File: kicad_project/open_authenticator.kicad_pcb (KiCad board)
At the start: 2 copper layers, 82 x 42 mm, 64 parts, among them IC1 TPS22919DCKR, J1 Conn_01x02_Female, J2 TYPE-C-31-M-17, J3 Conn_01x02_Female, P1 SSD1306_ribbon, Q1 DMP2305U-7, SW1 UP, SW2 DOWN, SW3 BOOT/SELECT, SW4 RESET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

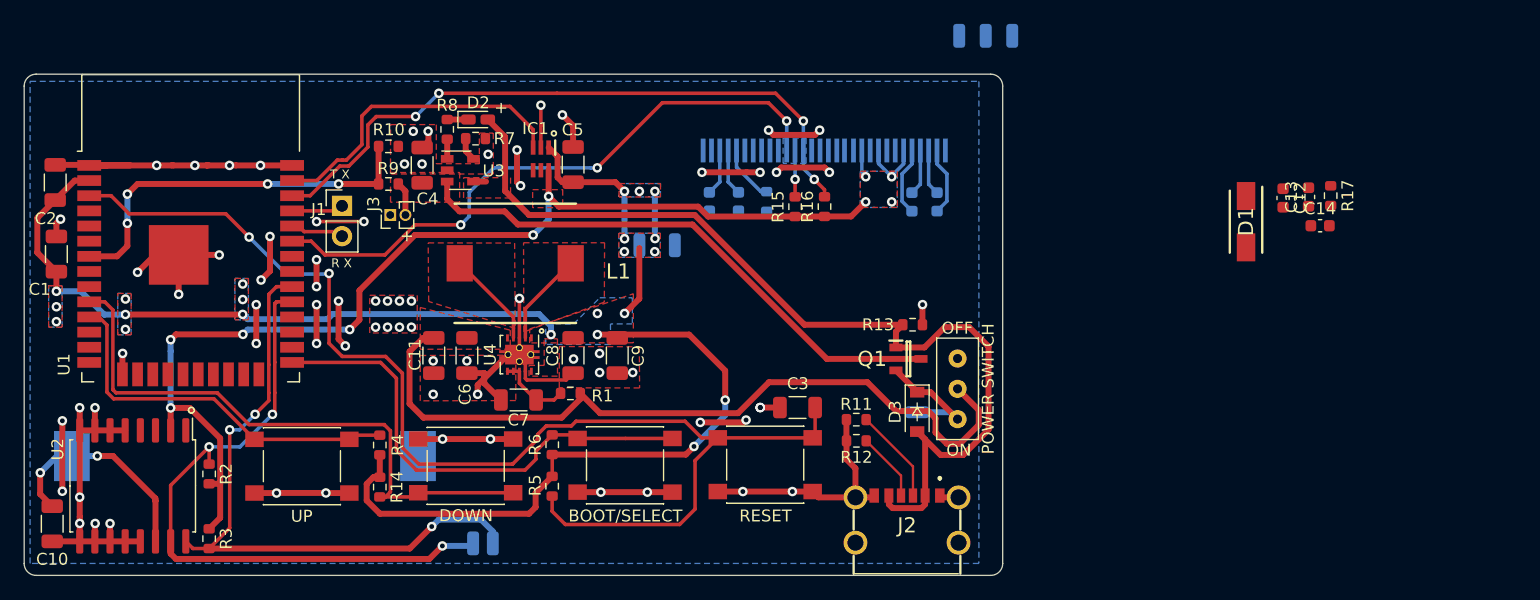
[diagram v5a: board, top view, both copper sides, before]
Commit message: Routed components of OLED sub circuit, optimised routing further (major: removed 3v3 line going under the regulator
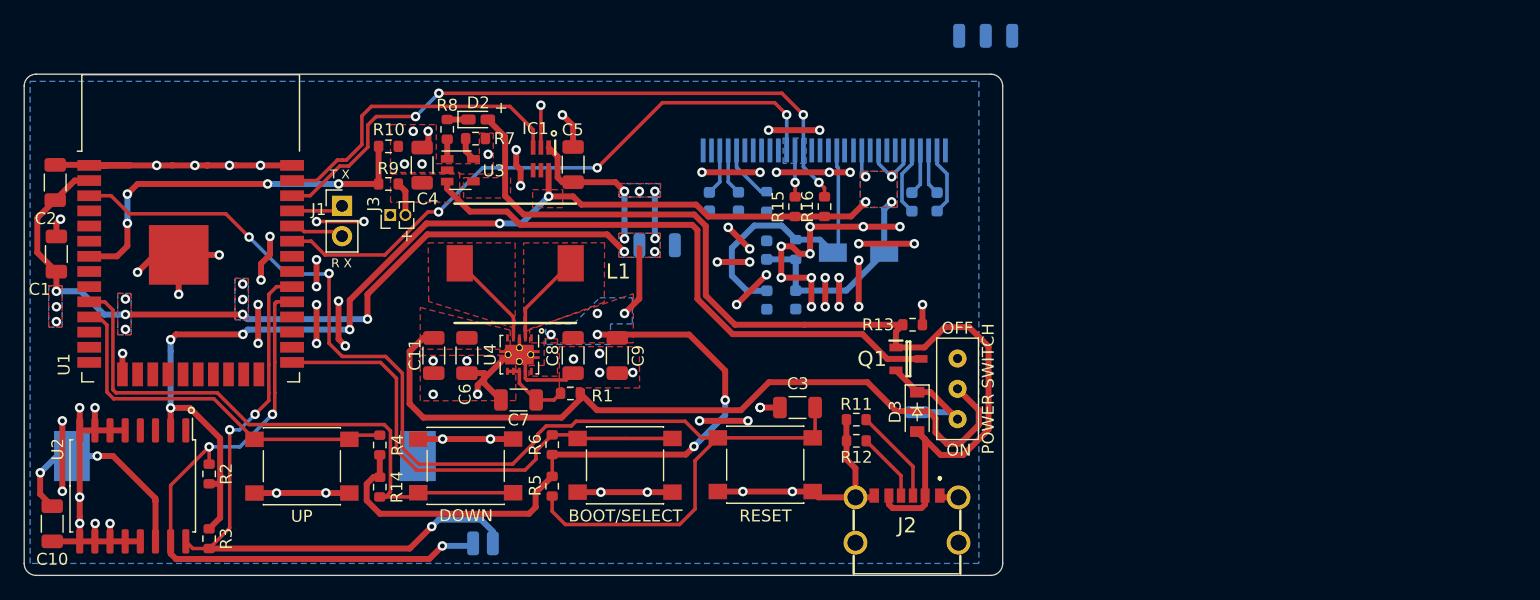
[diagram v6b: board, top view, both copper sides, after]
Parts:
- C12, C13, C14, D1, R17: moved to B.Cu
- moved C14 46.8 mm to (152.2, 98.9), turned to 90 degrees
- moved R17 45.1 mm to (154.7, 94.7), turned to 90 degrees
- moved C13 43.8 mm to (154.7, 98.9)
- moved C12 43.5 mm to (152.2, 94.7), turned to 90 degrees
- moved D1 32.6 mm to (159.9, 95.0), turned to 180 degrees
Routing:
- net GND: track 192.3 -> 232.6 mm, vias 74 -> 88
- net Net-(C14-Pad2): track 0.00 -> 24.8 mm
- net /LOAD_SWITCH_VCC: track 98.6 -> 115.7 mm
- net +3V3: track 135.3 -> 144.9 mm, vias 22 -> 23
- net +BATT: track 49.9 -> 52.8 mm
- net VBUS: track 82.0 -> 84.6 mm
- net /IO21_SDA: track 55.4 -> 54.5 mm

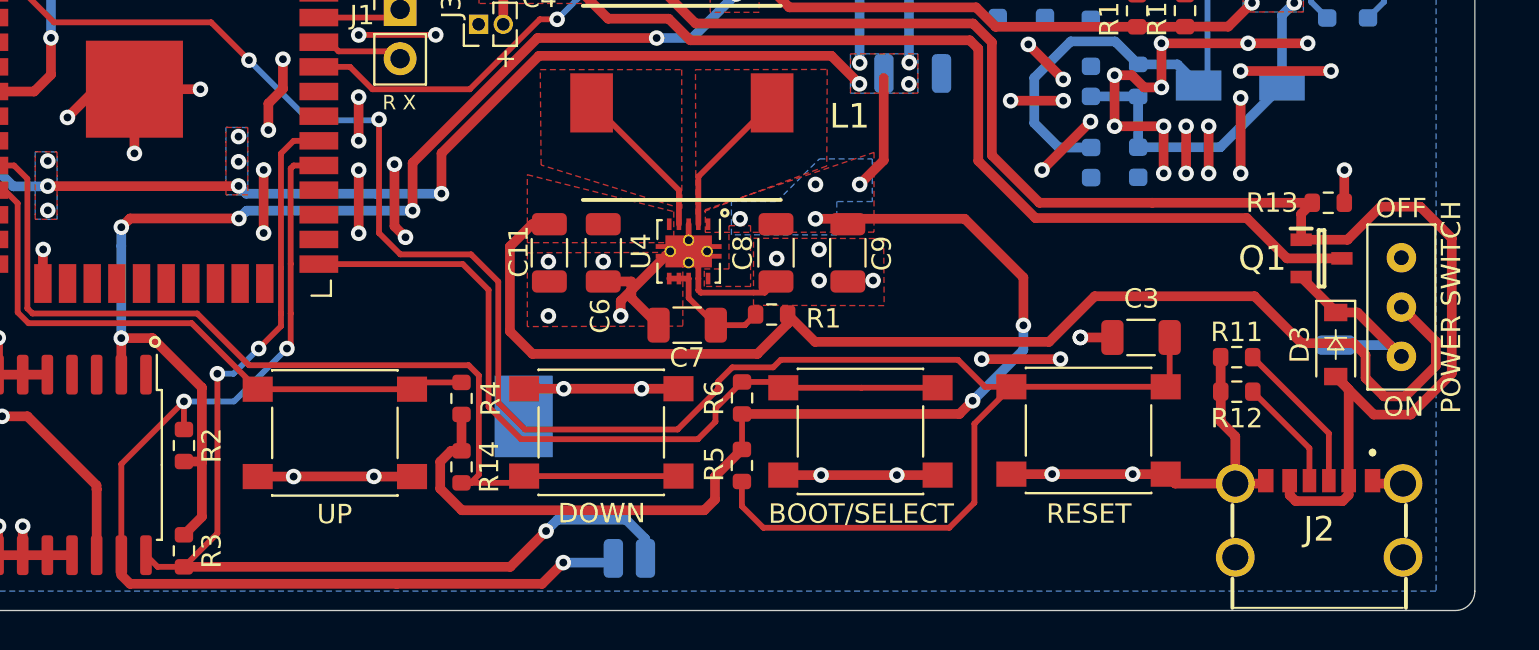
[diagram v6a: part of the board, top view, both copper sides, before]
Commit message: Optimised routing near slide switch
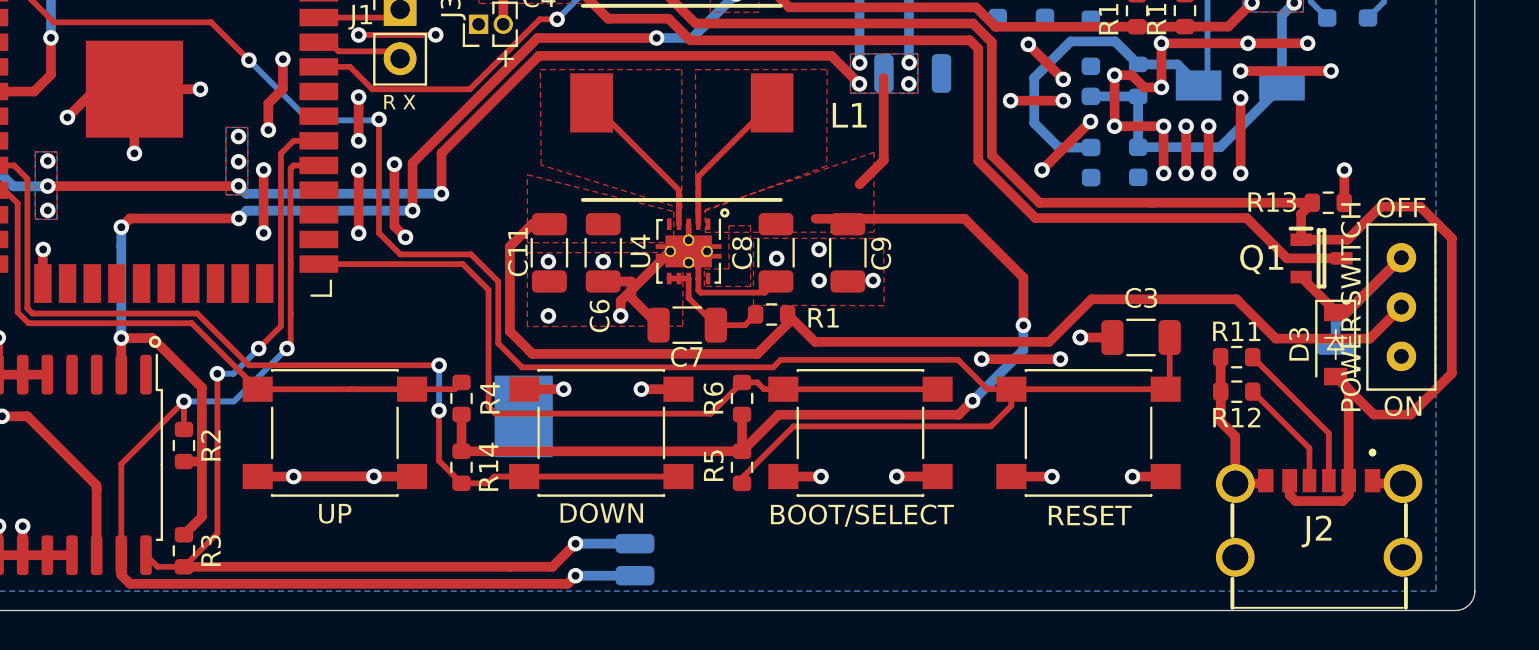
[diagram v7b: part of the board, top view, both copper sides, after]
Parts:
- moved TP2 1.42 mm to (128.7, 120.2), turned to 90 degrees
- moved TP3 0.93 mm to (128.7, 118.6), turned to 90 degrees
- moved SW4 0.12 mm to (152.1, 112.8)
- moved R5 0.09 mm to (134.2, 114.6)
- moved SW3 0.07 mm to (140.3, 112.8)
- turned SW5 to 0 degrees
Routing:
- net GND: track 232.6 -> 216.7 mm
- net /EN: track 103.6 -> 94.0 mm
- net Net-(C11-Pad1): track 65.0 -> 57.4 mm
- net +3V3: track 144.9 -> 139.4 mm, vias 23 -> 19
- net /V_INPUT: track 10.5 -> 13.0 mm
- net /IO18_SCL: track 54.5 -> 52.0 mm
- net /IO25: track 51.1 -> 49.3 mm, vias 0 -> 2
- net /BOOT: track 40.9 -> 39.8 mm
- net /IO5_SDA: track 55.1 -> 55.9 mm

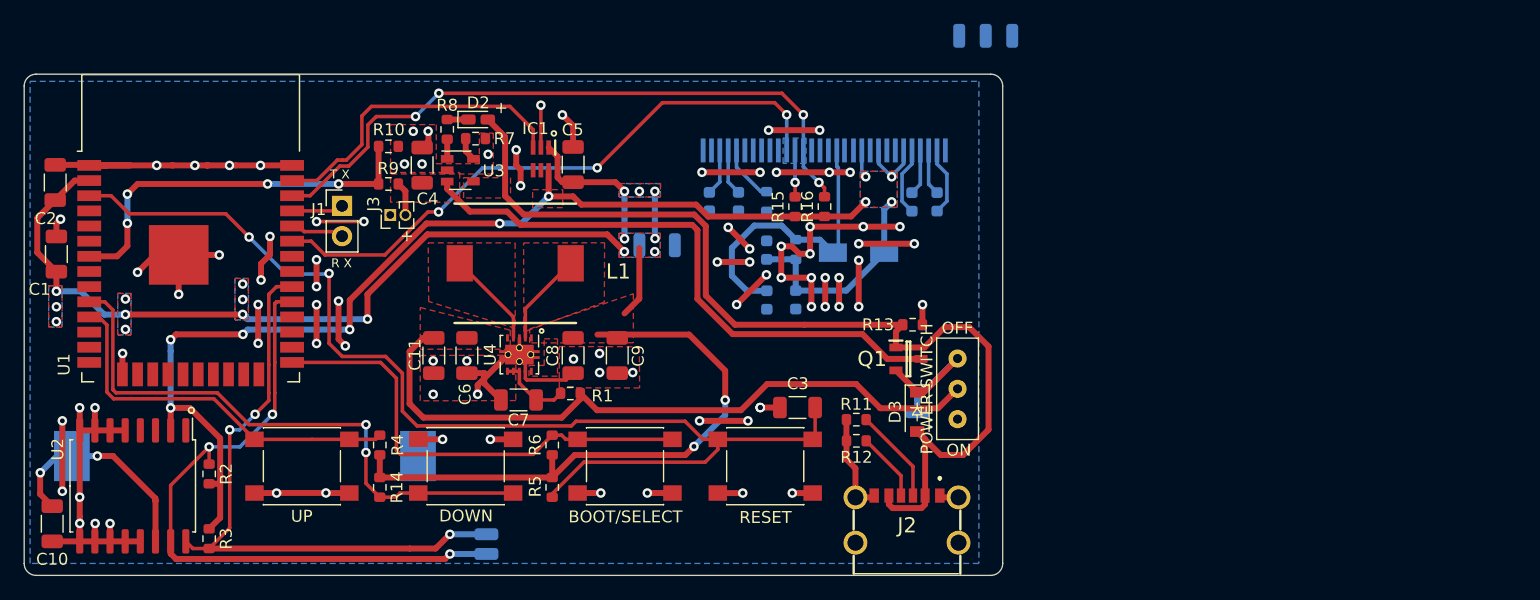
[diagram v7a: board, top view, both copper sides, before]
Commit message: Minor fix to routing and added artistic silkscreen drawings
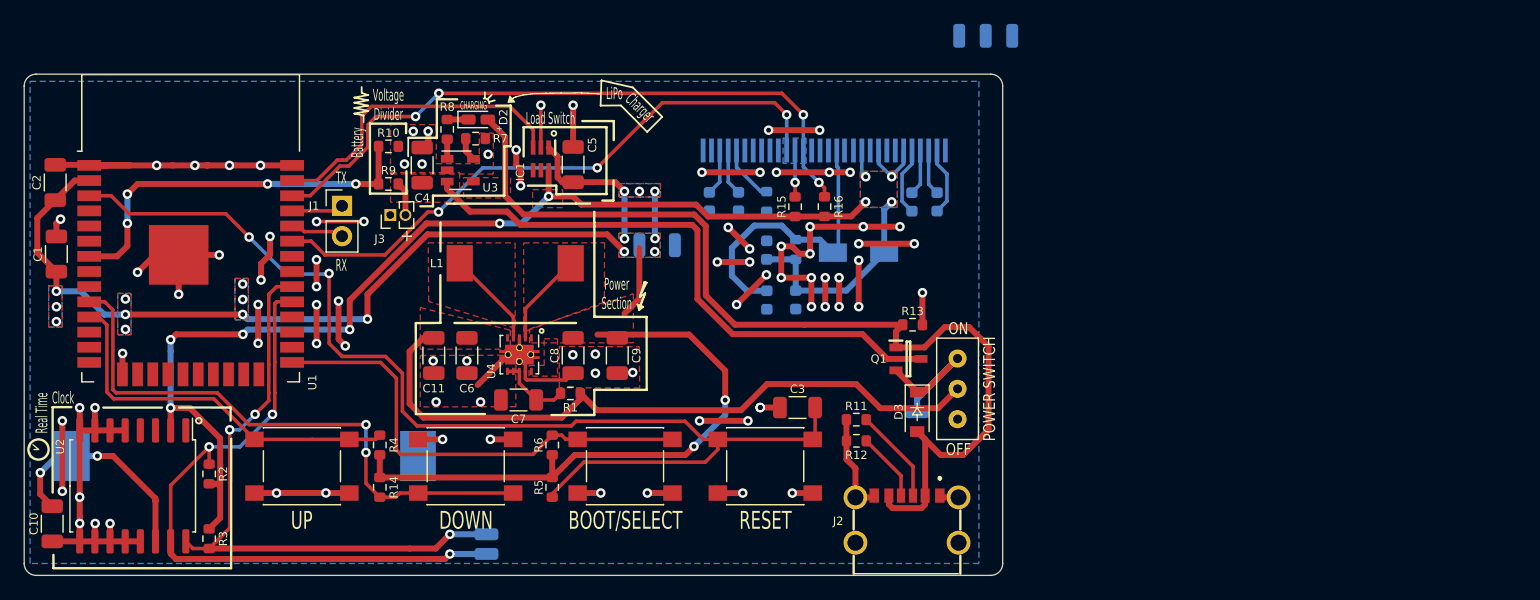
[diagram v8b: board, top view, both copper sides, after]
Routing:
- net GND: track 216.7 -> 213.1 mm
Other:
- board text added: "Battery"
- board text added: "CHARGING"
- board text added: "Charger"
- board text added: "Clock"
- board text added: "LiPo"
- board text added: "Load Switch"
- board text added: "Power Section"
- board text added: "RX"
- board text added: "Real Time"
- board text added: "TX"
- board text added: "Voltage Divider"
- board text removed: "R X"
- board text removed: "T X"
